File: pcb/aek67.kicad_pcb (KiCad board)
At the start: 2 copper layers, 304.8 x 100.4 mm, 35 parts, among them K13 =+, K14 BACK, K15 PAGE UP, K28 ]}, K29 \|, K30 PAGE DN, K42 ', K43 ENTER, K44 INSERT, K56 RSHIFT, K57 UP, K58 DEL, K62 SPACE, K64 RALT, K65 LEFT, K66 DOWN, K67 RIGHT, SW1 SW_PUSH, U1 ATmega32U4-AU, U2 PRTR5V0U2X, X1 XTAL_GND

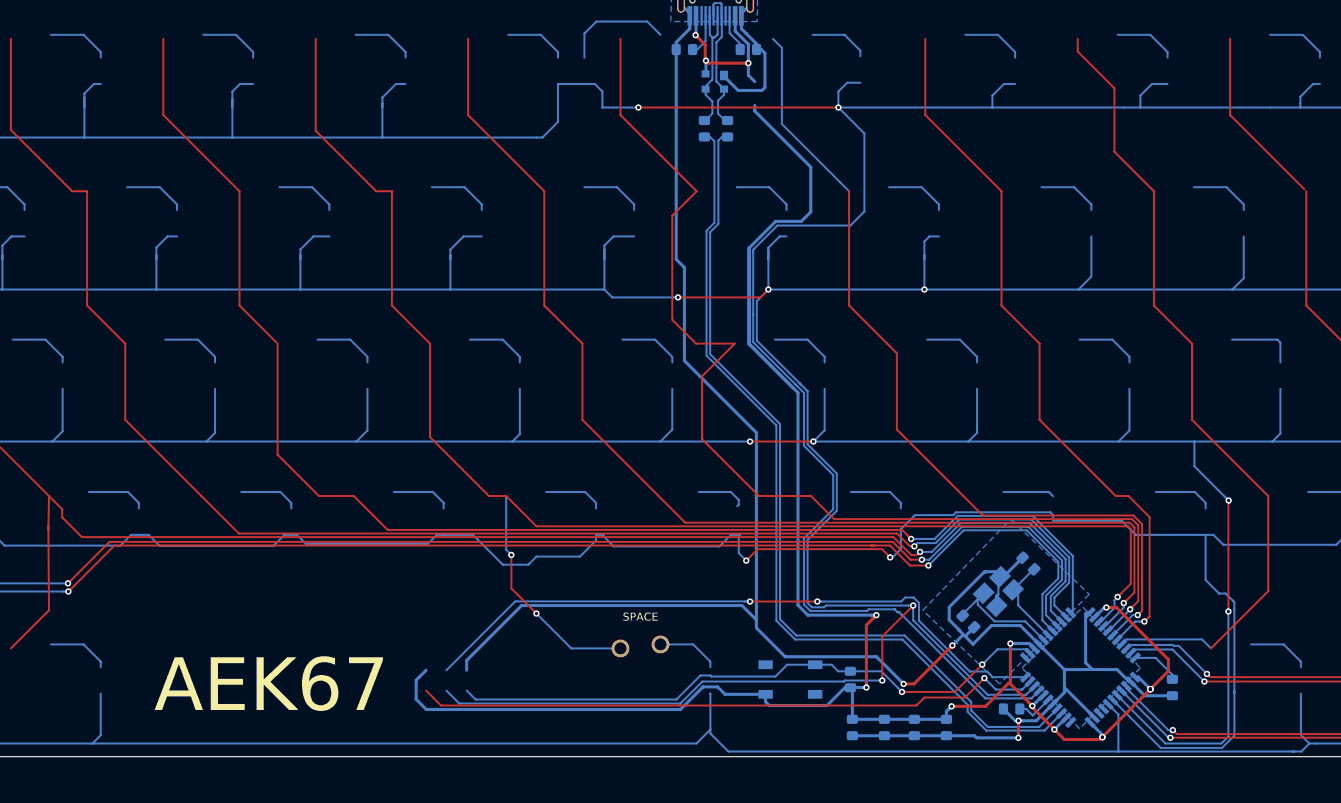
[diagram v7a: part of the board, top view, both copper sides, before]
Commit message: Fixed capacitor placement around MCU
and rerouted GND/Vcc to the MCU
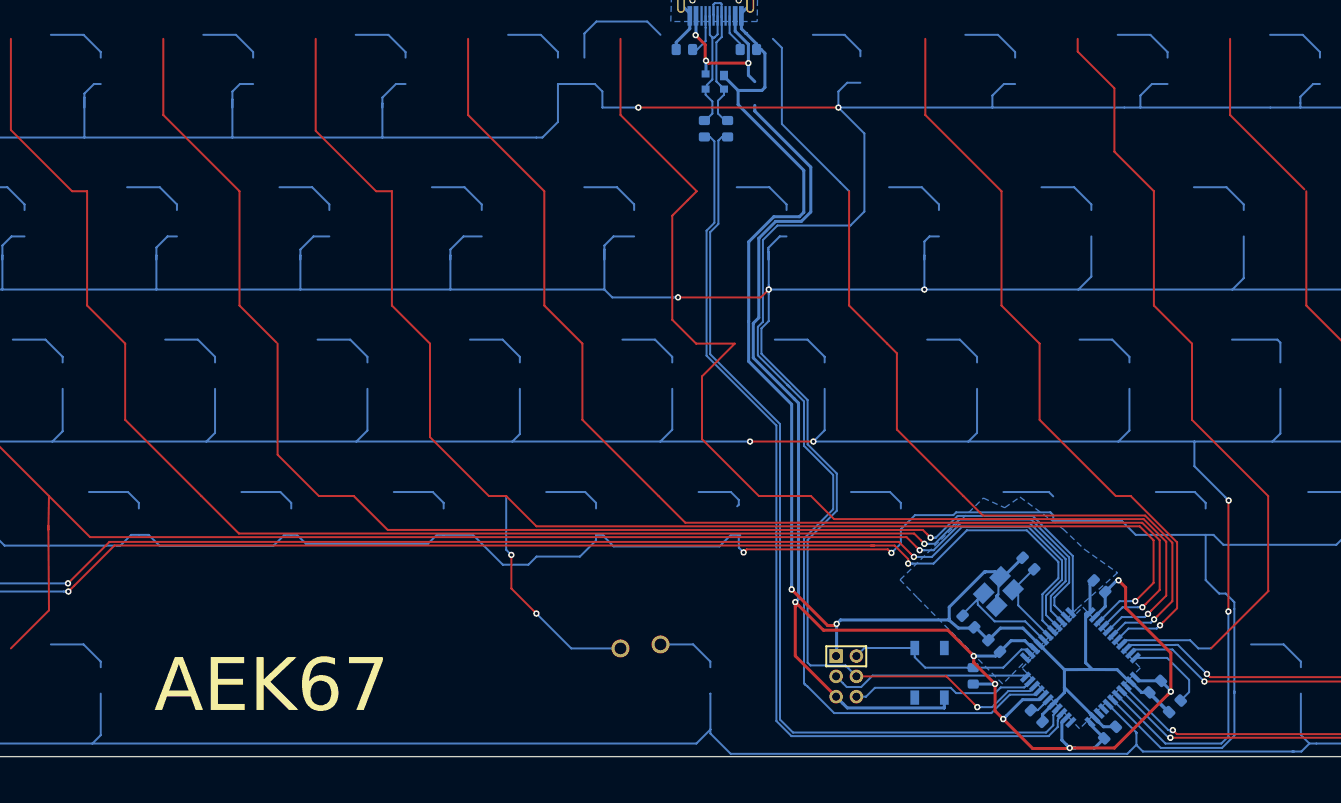
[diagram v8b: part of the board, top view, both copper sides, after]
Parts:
- added J1: AVR-ISP-6, random-keyboard-parts:Reset_Pretty-Mask, F.Cu at (189.2, 105.9)
- moved C3 34.2 mm to (227.8, 107.1), turned to 225 degrees
- moved C2 29.1 mm to (220.9, 94.6), turned to 135 degrees
- moved C4 20.5 mm to (222.2, 112.9), turned to 45 degrees
- moved C1 20.4 mm to (207.7, 102.1), turned to 135 degrees
- moved SW1 17.4 mm to (199.6, 105.4), turned to 270 degrees
- moved R1 15.4 mm to (205.1, 105.8)
- moved C7 3.26 mm to (213.0, 110.8), turned to 315 degrees
- moved R4 2.37 mm to (230.3, 109.6), turned to 45 degrees
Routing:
- net GND: track 303.4 -> 234.5 mm, vias 4 -> 2
- net SCLK: track 548.1 -> 485.0 mm, vias 5 -> 4
- net MOSI: track 81.7 -> 24.9 mm, vias 2 -> 0
- net MISO: track 79.4 -> 24.4 mm, vias 1 -> 0
- net RST: track 77.3 -> 25.9 mm, vias 2 -> 0
- net +5V: track 260.8 -> 220.8 mm, vias 13 -> 7
- net Net-(R2-Pad1): track 107.0 -> 115.2 mm
- net Net-(R3-Pad1): track 108.2 -> 116.3 mm
- net row0: track 491.2 -> 497.7 mm
- net col8: track 106.6 -> 112.1 mm
- net col7: track 136.8 -> 142.2 mm
- net col6: track 142.2 -> 147.0 mm
- net Net-(R4-Pad2): track 6.09 -> 10.9 mm
- net col9: track 90.0 -> 94.4 mm
- net col5: track 191.1 -> 195.4 mm
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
